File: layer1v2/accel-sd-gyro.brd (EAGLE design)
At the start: 17.8 x 49.5 mm, 17 parts, among them IC2 LGD20H, U1 MMA8452Q, U2 microSD

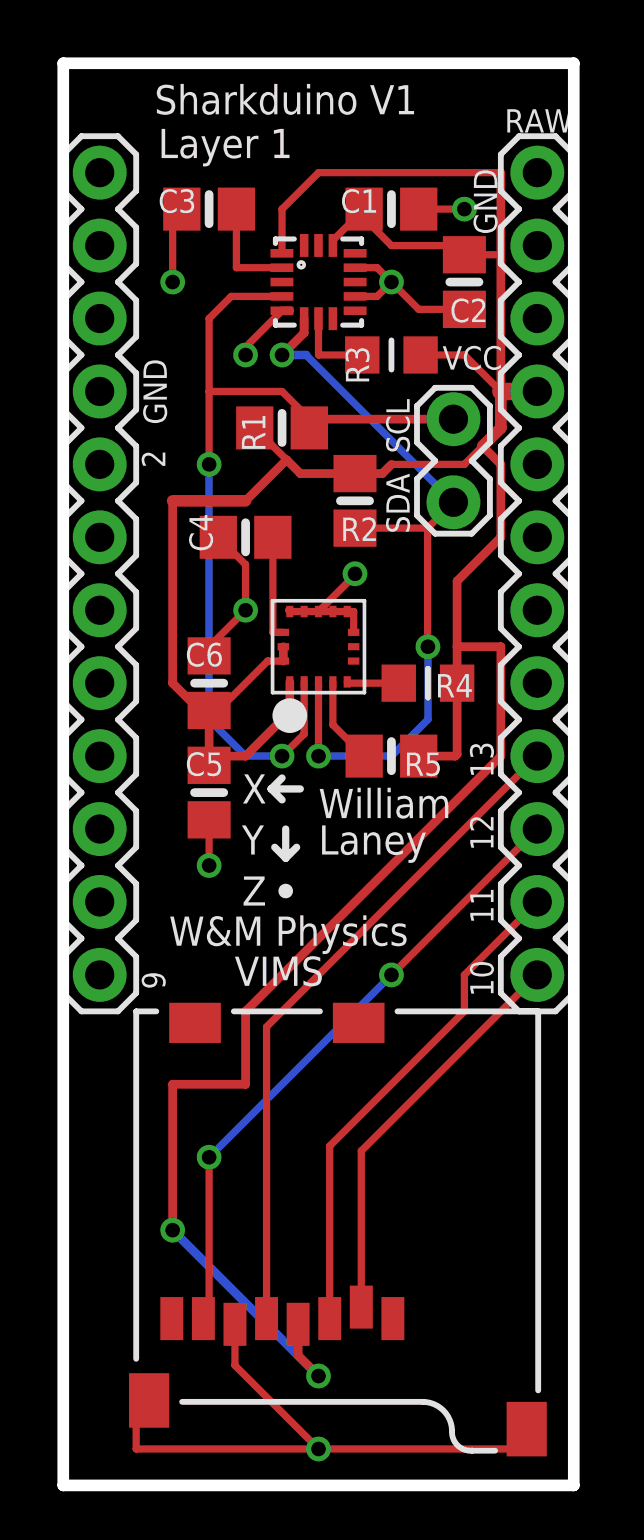
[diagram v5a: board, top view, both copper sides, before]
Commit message: silk screen
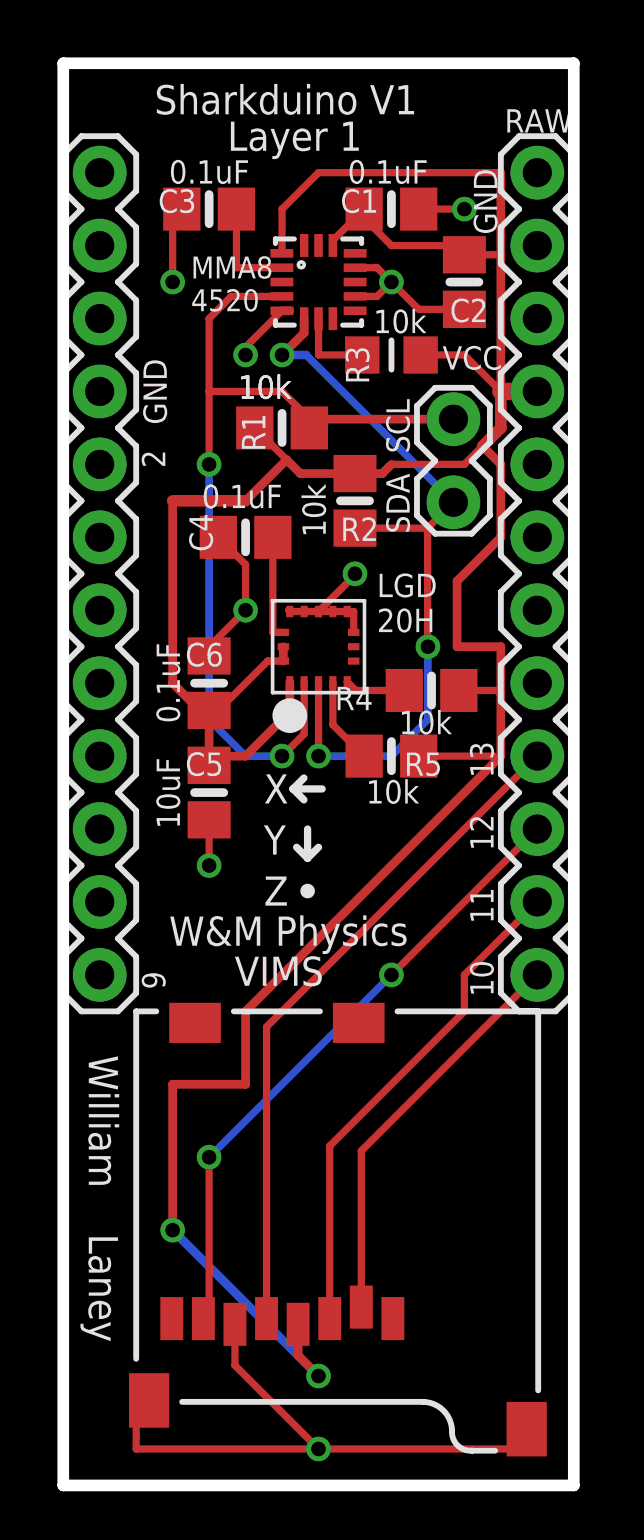
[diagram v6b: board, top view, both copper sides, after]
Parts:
- R4: device microbuilder:_0805MP -> microbuilder:0805-NO
- moved R4 0.28 mm to (12.8, 27.7)
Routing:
- net +3V3: track 113.9 -> 113.1 mm
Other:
- board text added: "0.1uF"
- board text added: "10k"
- board text added: "10uF"
- board text added: "LGD 20H"
- board text added: "MMA8 4520"
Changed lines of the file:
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@@
 <setting verticaltext="up"/>
 </settings>
-<grid distance="0.05" unitdist="inch" unit="inch" style="lines" multiple="1" display="yes" altdistance="0.005" altunitdist="inch" altunit="inch"/>
+<grid distance="0.005" unitdist="inch" unit="inch" style="lines" multiple="1" display="yes" altdistance="0.005" altunitdist="inch" altunit="inch"/>
 <layers>
 <layer number="1" name="Top" color="4" fill="1" visible="yes" active="yes"/>
@@
 <layer number="21" name="tPlace" color="16" fill="1" visible="yes" active="yes"/>
 <layer number="22" name="bPlace" color="14" fill="1" visible="yes" active="yes"/>
-<layer number="23" name="tOrigins" color="15" fill="1" visible="no" active="yes"/>
-<layer number="24" name="bOrigins" color="15" fill="1" visible="no" active="yes"/>
+<layer number="23" name="tOrigins" color="15" fill="1" visible="yes" active="yes"/>
+<layer number="24" name="bOrigins" color="15" fill="1" visible="yes" active="yes"/>
 <layer number="25" name="tNames" color="7" fill="1" visible="no" active="yes"/>
 <layer number="26" name="bNames" color="7" fill="1" visible="no" active="yes"/>
@@
 <wire x1="17.78" y1="49.53" x2="17.78" y2="0" width="0.4064" layer="20"/>
 <wire x1="0" y1="0" x2="17.78" y2="0" width="0.4064" layer="20"/>
-<wire x1="7.747" y1="21.844" x2="7.747" y2="22.86" width="0.254" layer="21"/>
-<wire x1="7.747" y1="21.844" x2="8.128" y2="22.225" width="0.254" layer="21"/>
-<wire x1="7.747" y1="21.844" x2="7.366" y2="22.225" width="0.254" layer="21"/>
-<wire x1="7.239" y1="24.257" x2="8.255" y2="24.257" width="0.254" layer="21"/>
-<wire x1="7.239" y1="24.257" x2="7.62" y2="23.876" width="0.254" layer="21"/>
-<wire x1="7.239" y1="24.257" x2="7.62" y2="24.638" width="0.254" layer="21"/>
-<circle x="7.747" y="20.701" radius="0.127" width="0.254" layer="21"/>
-<text x="6.223" y="23.749" size="1.016" layer="21" font="vector" ratio="15">X</text>
-<text x="6.223" y="21.971" size="1.016" layer="21" font="vector" ratio="15">Y</text>
-<text x="6.223" y="20.193" size="1.016" layer="21" font="vector" ratio="15">Z</text>
+<wire x1="8.509" y1="21.844" x2="8.509" y2="22.86" width="0.254" layer="21"/>
+<wire x1="8.509" y1="21.844" x2="8.89" y2="22.225" width="0.254" layer="21"/>
+<wire x1="8.509" y1="21.844" x2="8.128" y2="22.225" width="0.254" layer="21"/>
+<wire x1="8.001" y1="24.257" x2="9.017" y2="24.257" width="0.254" layer="21"/>
+<wire x1="8.001" y1="24.257" x2="8.382" y2="23.876" width="0.254" layer="21"/>
+<wire x1="8.001" y1="24.257" x2="8.382" y2="24.638" width="0.254" layer="21"/>
+<circle x="8.509" y="20.701" radius="0.127" width="0.254" layer="21"/>
+<text x="6.985" y="23.749" size="1.016" layer="21" font="vector" ratio="15">X</text>
+<text x="6.985" y="21.971" size="1.016" layer="21" font="vector" ratio="15">Y</text>
+<text x="6.985" y="20.193" size="1.016" layer="21" font="vector" ratio="15">Z</text>
 <text x="12.065" y="33.147" size="0.8128" layer="21" font="vector" ratio="15" rot="R90">SDA</text>
 <text x="12.065" y="35.941" size="0.8128" layer="21" font="vector" ratio="15" rot="R90">SCL</text>
@@
 <text x="15.113" y="43.561" size="0.8128" layer="21" font="vector" ratio="15" rot="R90">GND</text>
 <text x="13.208" y="38.862" size="0.8128" layer="21" font="vector" ratio="15">VCC</text>
-<text x="8.89" y="23.241" size="1.016" layer="21" font="vector" ratio="15">William</text>
-<text x="8.89" y="21.971" size="1.016" layer="21" font="vector" ratio="15">Laney</text>
+<text x="0.889" y="14.986" size="1.016" layer="21" font="vector" ratio="15" rot="SR270">William</text>
+<text x="0.889" y="8.763" size="1.016" layer="21" font="vector" ratio="15" rot="SR270">Laney</text>
 <text x="3.175" y="47.752" size="1.016" layer="21" font="vector" ratio="15">Sharkduino V1</text>
-<text x="3.302" y="46.228" size="1.016" layer="21" font="vector" ratio="15">Layer 1</text>
+<text x="5.715" y="46.482" size="1.016" layer="21" font="vector" ratio="15">Layer 1</text>
 <text x="3.556" y="35.433" size="0.8128" layer="21" font="vector" ratio="15" rot="R90">2</text>
 <text x="15.367" y="47.117" size="0.8128" layer="21" font="vector" ratio="15">RAW</text>
 <text x="3.683" y="18.796" size="1.016" layer="21" font="vector" ratio="15">W&amp;M Physics</text>
 <text x="5.969" y="17.399" size="1.016" layer="21" font="vector" ratio="15">VIMS</text>
+<text x="4.064" y="22.86" size="0.8128" layer="21" font="vector" ratio="15" rot="R90">10uF</text>
+<text x="4.064" y="26.543" size="0.8128" layer="21" font="vector" ratio="15" rot="R90">0.1uF</text>
+<text x="4.826" y="34.036" size="0.8128" layer="21" font="vector" ratio="15">0.1uF</text>
+<text x="6.096" y="37.846" size="0.8128" layer="21" font="vector" ratio="15">10k</text>
+<text x="9.144" y="33.02" size="0.8128" layer="21" font="vector" ratio="15" rot="R90">10k</text>
+<text x="11.684" y="26.162" size="0.8128" layer="21" font="vector" ratio="15">10k</text>
+<text x="10.541" y="23.749" size="0.8128" layer="21" font="vector" ratio="15">10k</text>
+<text x="3.683" y="45.339" size="0.8128" layer="21" font="vector" ratio="15">0.1uF</text>
+<text x="9.906" y="45.339" size="0.8128" layer="21" font="vector" ratio="15">0.1uF</text>
+<text x="10.795" y="40.132" size="0.8128" layer="21" font="vector" ratio="15">10k</text>
+<text x="6.096" y="37.846" size="0.8128" layer="21" font="vector" ratio="15">10k</text>
+<text x="10.922" y="29.718" size="0.8128" layer="21" font="vector" ratio="15">LGD
+20H</text>
+<text x="4.445" y="40.894" size="0.762" layer="21" font="vector" ratio="15">MMA8
+4520</text>
 </plain>
 <attributes>
@@
 <attribute name="VALUE" x="5.588" y="37.465" size="0.4064" layer="27" ratio="10" rot="R270"/>
 </element>
-<element name="R4" library="microbuilder" package="_0805MP" value="10K" x="12.7" y="27.94" smashed="yes" rot="R180">
-<attribute name="NAME" x="14.2875" y="28.2575" size="0.8128" layer="25" ratio="18" rot="R180"/>
-<attribute name="VALUE" x="10.668" y="28.5115" size="0.4064" layer="27" ratio="10" rot="R270"/>
-</element>
 <element name="R5" library="microbuilder" package="0805-NO" value="10K" x="11.43" y="25.4" smashed="yes" rot="R180">
 <attribute name="NAME" x="13.208" y="25.527" size="0.8128" layer="25" ratio="18" rot="R180"/>
@@
 <attribute name="VALUE" x="13.208" y="39.878" size="0.4064" layer="27" ratio="10"/>
 </element>
+<element name="R4" library="microbuilder" package="0805-NO" value="10K" x="12.827" y="27.686" rot="R180"/>
 </elements>
 <signals>
@@
 <contactref element="R1" pad="2"/>
 <contactref element="R2" pad="1"/>
-<contactref element="R4" pad="1"/>
 <contactref element="C5" pad="2"/>
 <contactref element="C6" pad="2"/>
@@
 <wire x1="7.665" y1="28.71" x2="7.12" y2="28.71" width="0.254" layer="1"/>
 <wire x1="7.12" y1="28.71" x2="5.08" y2="26.67" width="0.254" layer="1"/>
-<wire x1="13.716" y1="27.94" x2="13.716" y2="25.466" width="0.3048" layer="1"/>
 <wire x1="10.16" y1="35.24" x2="11.11" y2="35.24" width="0.3048" layer="1"/>
 <wire x1="11.11" y1="35.24" x2="11.43" y2="35.56" width="0.3048" layer="1"/>
@@
 <wire x1="3.81" y1="34.29" x2="6.35" y2="34.29" width="0.4064" layer="1"/>
 <wire x1="6.35" y1="34.29" x2="7.78" y2="35.72" width="0.3048" layer="1"/>
-<wire x1="13.716" y1="27.94" x2="13.716" y2="29.21" width="0.3048" layer="1"/>
 <wire x1="13.716" y1="29.21" x2="13.716" y2="31.496" width="0.3048" layer="1"/>
 <wire x1="13.716" y1="31.496" x2="15.24" y2="33.02" width="0.3048" layer="1"/>
@@
 <wire x1="9.39" y1="43.36" x2="10.48" y2="44.45" width="0.254" layer="1"/>
 <wire x1="13.97" y1="39.37" x2="15.24" y2="38.1" width="0.254" layer="1"/>
-<wire x1="15.24" y1="25.4" x2="15.24" y2="29.21" width="0.3048" layer="1"/>
+<wire x1="15.24" y1="25.4" x2="15.24" y2="27.559" width="0.3048" layer="1"/>
+<wire x1="15.24" y1="27.559" x2="15.24" y2="29.21" width="0.3048" layer="1"/>
 <wire x1="15.24" y1="29.21" x2="13.716" y2="29.21" width="0.3048" layer="1"/>
-<wire x1="12.38" y1="25.4" x2="13.65" y2="25.4" width="0.3048" layer="1"/>
-<wire x1="13.65" y1="25.4" x2="13.716" y2="25.466" width="0.3048" layer="1"/>
-<wire x1="15.24" y1="25.4" x2="6.35" y2="16.51" width="0.3048" layer="1"/>
+<wire x1="15.24" y1="25.4" x2="15.113" y2="25.273" width="0.3048" layer="1"/>
+<wire x1="15.113" y1="25.273" x2="6.35" y2="16.51" width="0.3048" layer="1"/>
 <wire x1="6.35" y1="16.51" x2="6.35" y2="13.97" width="0.3048" layer="1"/>
 <wire x1="6.35" y1="13.97" x2="3.81" y2="13.97" width="0.3048" layer="1"/>
 <wire x1="3.81" y1="13.97" x2="3.81" y2="8.89" width="0.3048" layer="1"/>
+<contactref element="R4" pad="1"/>
+<wire x1="13.777" y1="27.686" x2="15.113" y2="27.686" width="0.254" layer="1"/>
+<wire x1="15.113" y1="27.686" x2="15.24" y2="27.559" width="0.254" layer="1"/>
+<wire x1="12.38" y1="25.4" x2="14.986" y2="25.4" width="0.254" layer="1"/>
+<wire x1="14.986" y1="25.4" x2="15.113" y2="25.273" width="0.254" layer="1"/>
 </signal>
 <signal name="CS_3.3V">
+<contactref element="IC2" pad="5"/>
+<wire x1="9.935" y1="27.94" x2="9.89" y2="27.985" width="0.254" layer="1"/>
 <contactref element="R4" pad="2"/>
-<contactref element="IC2" pad="5"/>
-<wire x1="11.684" y1="27.94" x2="9.935" y2="27.94" width="0.254" layer="1"/>
-<wire x1="9.935" y1="27.94" x2="9.89" y2="27.985" width="0.254" layer="1"/>
+<wire x1="11.877" y1="27.686" x2="10.189" y2="27.686" width="0.254" layer="1"/>
+<wire x1="10.189" y1="27.686" x2="9.89" y2="27.985" width="0.254" layer="1"/>
 </signal>
 <signal name="N$6">
@@
 </board>
 </drawing>
+<compatibility>
+<note version="6.3" minversion="6.2.2" severity="warning">
+Since Version 6.2.2 text objects can contain more than one line,
+which will not be processed correctly with this version.
+</note>
+</compatibility>
 </eagle>
